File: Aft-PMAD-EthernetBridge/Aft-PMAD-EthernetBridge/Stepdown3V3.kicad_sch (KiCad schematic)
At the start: 7 parts, among them U3 TPS564257DRLR

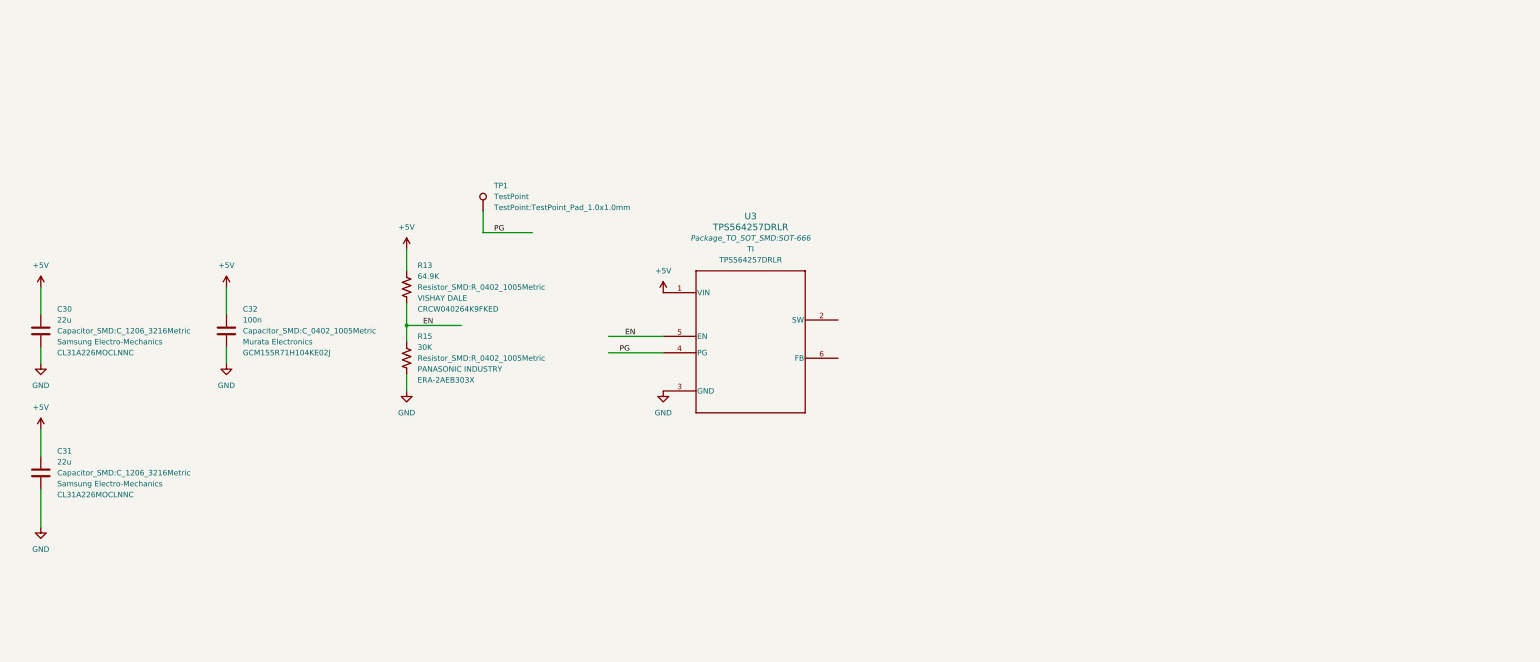
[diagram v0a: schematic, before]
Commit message: update minor changes to 24vdc Step down (change resistor from 240K-ish to 10K) complete 3v3 stepdown
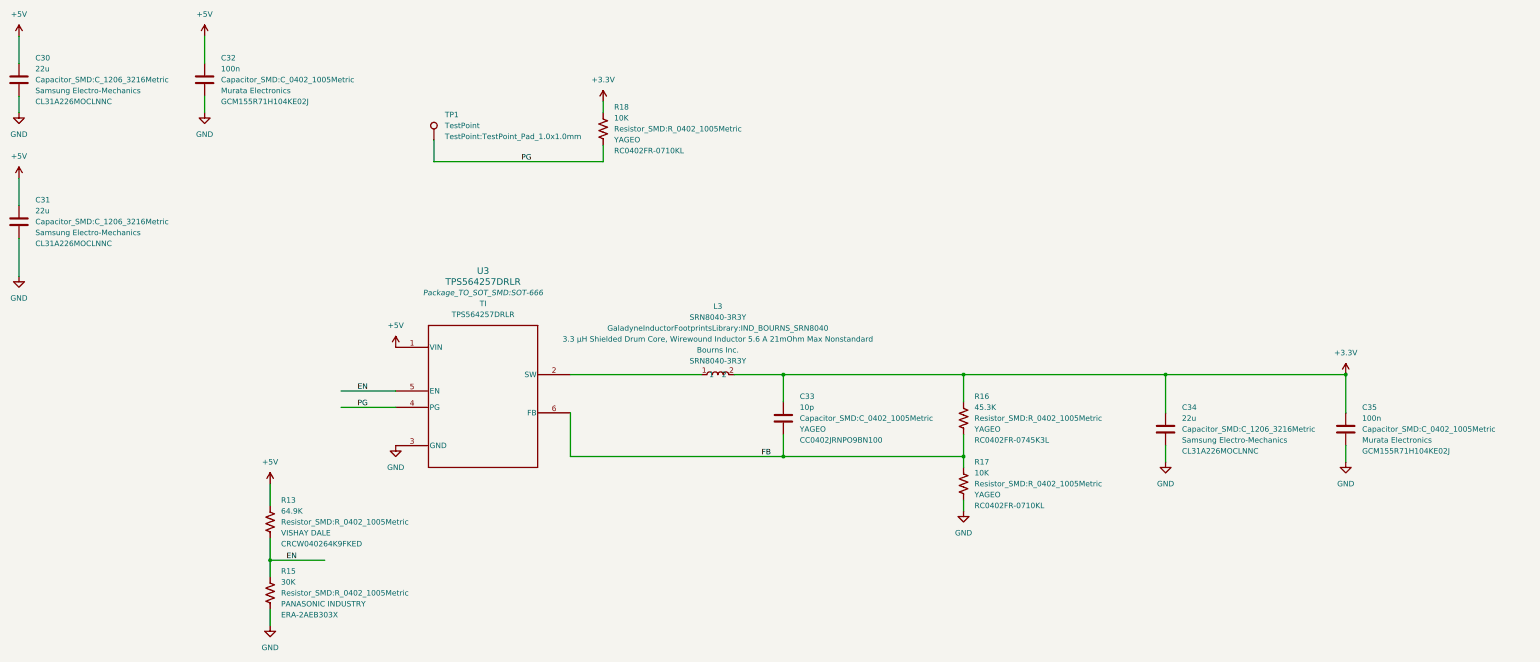
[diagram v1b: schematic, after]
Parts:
- added C33: 10p, Capacitor_SMD:C_0402_1005Metric, symbol Device:C
- added C34: 22u, Capacitor_SMD:C_1206_3216Metric, symbol Device:C
- added C35: 100n, Capacitor_SMD:C_0402_1005Metric, symbol Device:C
- added L3: SRN8040-3R3Y, GaladyneInductorFootprintsLibrary:IND_BOURNS_SRN8040, symbol GaladyneInductorsLibrary:SRN8040-3R3Y
- added R16: 45.3K, Resistor_SMD:R_0402_1005Metric, symbol Device:R_US
- added R17, R18: 10K, Resistor_SMD:R_0402_1005Metric, symbol Device:R_US
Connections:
- net GND: now also C34.2, C35.2, R17.2
- net PG: now also R18.2
- net at U3.2 (SW): now also L3.1
- net FB: now reaches U3.6 (FB)
- net FB: now also C33.2, R16.2, R17.1
- new net +3.3V: C33.1, C34.1, C35.1, L3.2, R16.1, R18.1
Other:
- moved on the sheet: C30, C31, C32, R13, R15, TP1, U3
